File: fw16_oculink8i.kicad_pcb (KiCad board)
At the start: 4 copper layers, 99.3 x 73.9 mm, 78 parts, among them J1 FXBeam, J2 x8 NPIO, J3 USB_A, J4 FAN_CON_L, J5 FAN_CON_R, SW1 SW_DPDT_x2, SW2 SW_DPDT_x2, U1 LM393, U2 BR24G32FVT-3GE2

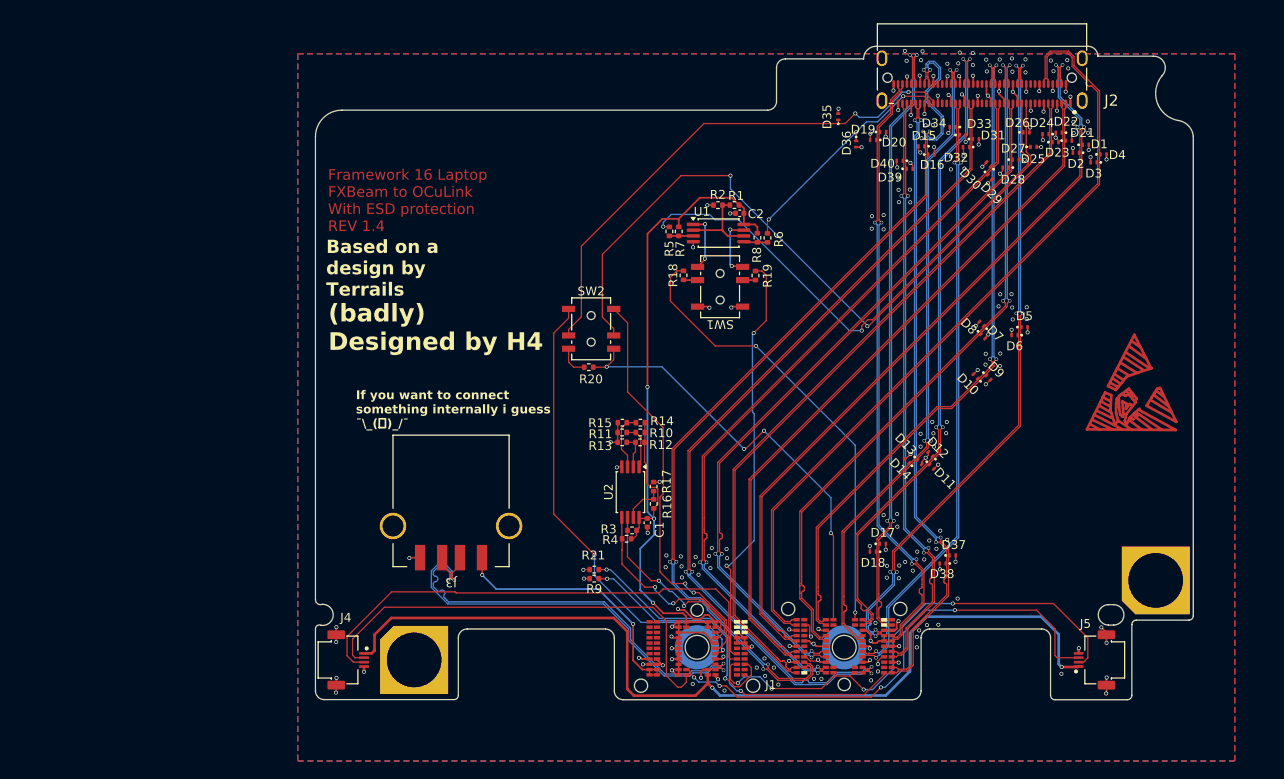
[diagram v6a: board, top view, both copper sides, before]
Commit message: updated routing for JLC04121H-7628 1.2mm PCBs
Because this stackup lets you have cheaper PCBAs.
A bit bigger traces but it should be fine.
Passes ERC, needs a bit more GND vias scattered around.
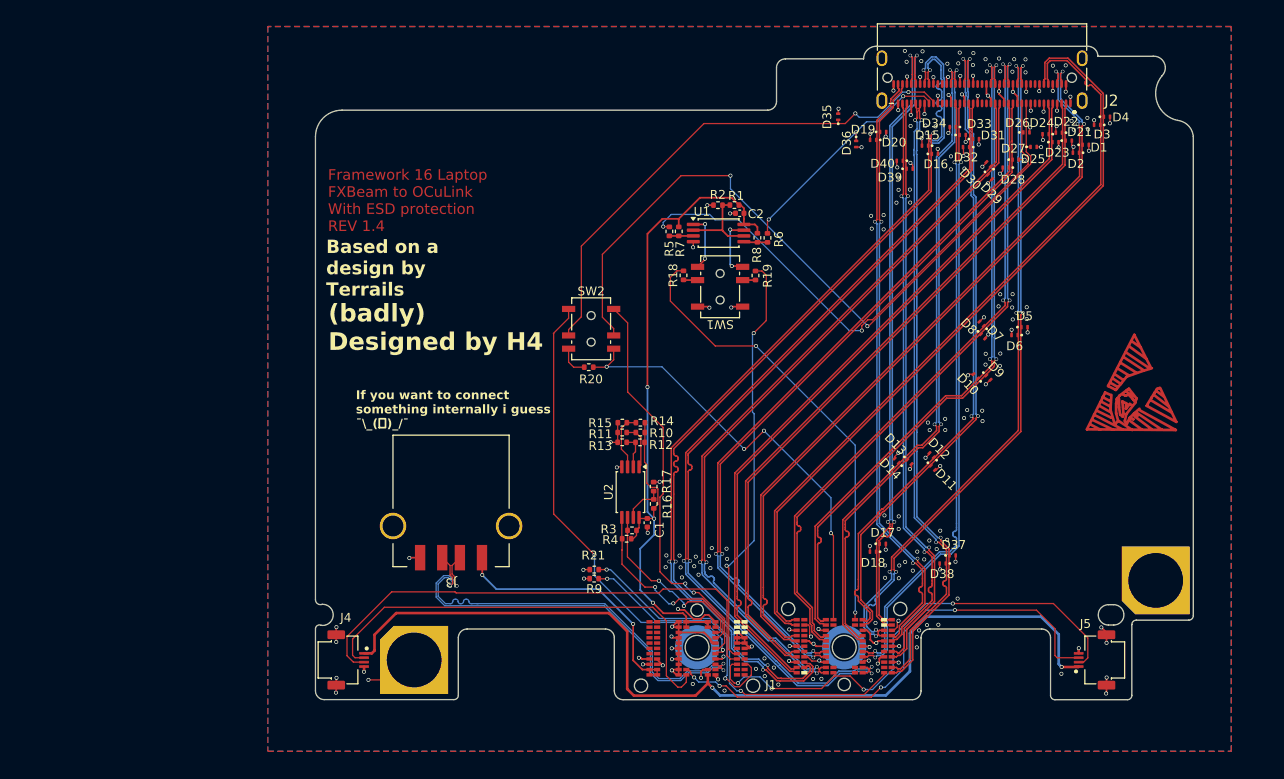
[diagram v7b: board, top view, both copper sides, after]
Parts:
- moved D4 4.28 mm to (145.9, 31.2)
- moved D3 4.26 mm to (144.8, 32.1)
- moved D14 1.16 mm to (122.2, 70.1)
- moved D13 1.16 mm to (123.6, 70.3)
- moved D15 0.41 mm to (125.4, 34.5)
- moved D16 0.41 mm to (126.5, 35.4)
- moved D11 0.18 mm to (126.2, 70.9)
- moved D12 0.18 mm to (126.1, 69.5)
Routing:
- net GND: track 133.0 -> 138.4 mm, vias 218 -> 219
- net /REFCLKB+: track 100.5 -> 103.7 mm
- net /RX1+: track 89.3 -> 87.6 mm
- net /RX1-: track 89.3 -> 87.6 mm
- net /RX0-: track 86.2 -> 84.6 mm
- net /RX0+: track 86.2 -> 84.6 mm
- net /REFCLKB-: track 103.0 -> 103.9 mm
- net /TX5+: track 68.7 -> 69.4 mm
- net /TX5-: track 68.6 -> 69.4 mm
- net /RX2+: track 78.9 -> 79.5 mm
- net /RX2-: track 79.0 -> 79.6 mm

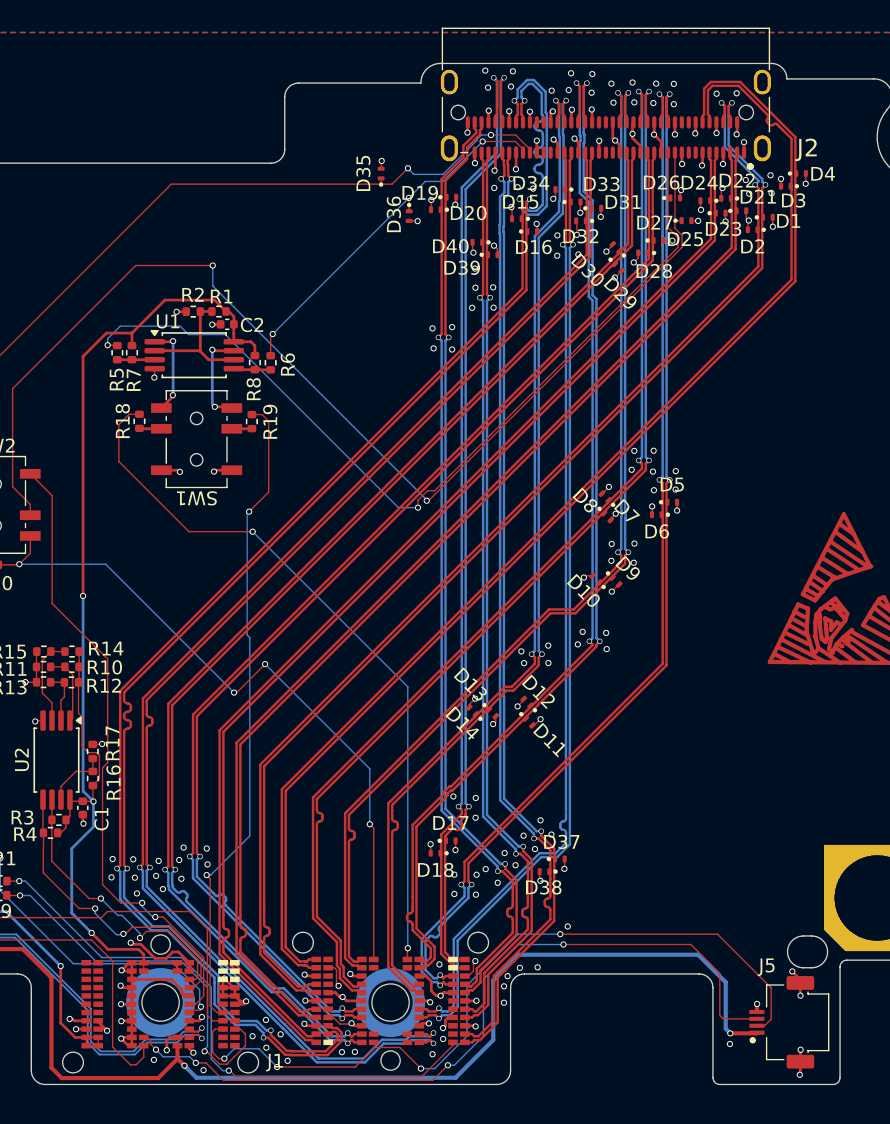
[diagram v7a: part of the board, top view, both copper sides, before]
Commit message: added a whole lot of GND vias
because high frequency so better off playing it safe and annoy JLCPCB production a bit.
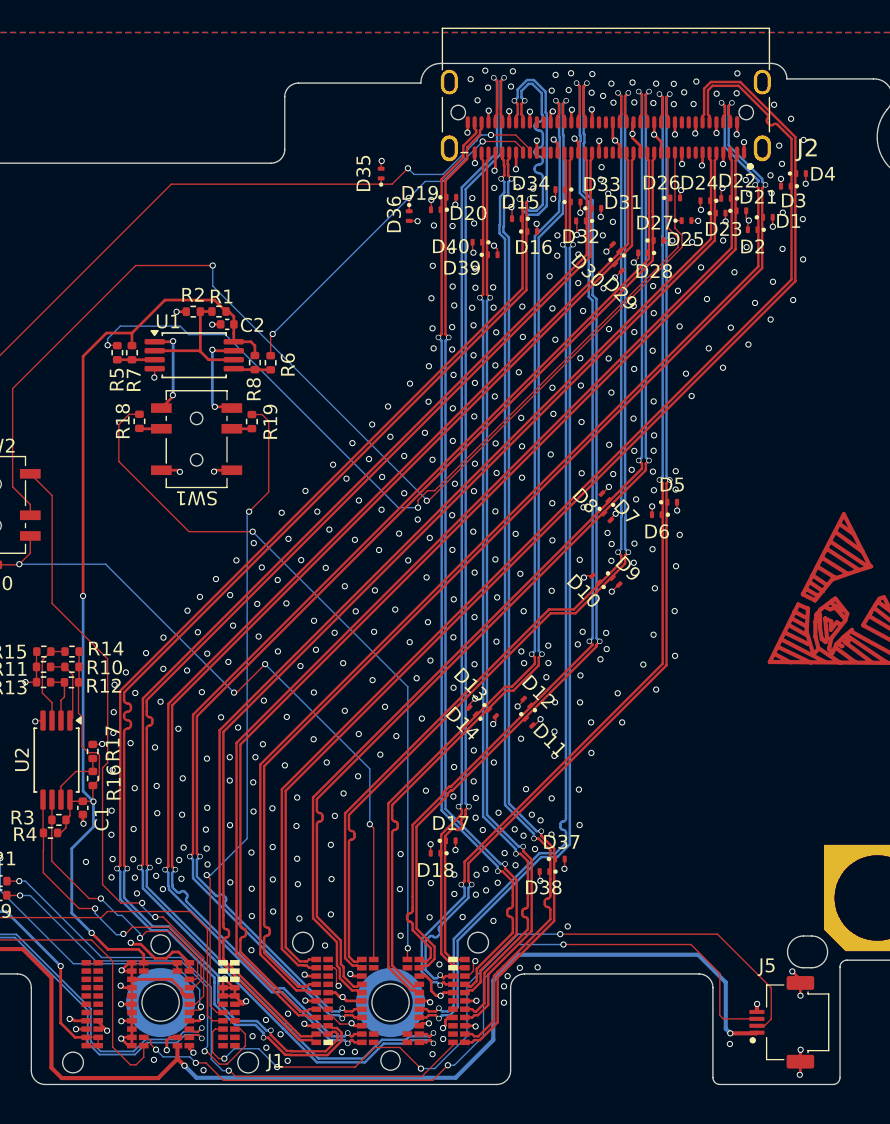
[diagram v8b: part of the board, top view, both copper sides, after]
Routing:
- net GND: vias 219 -> 513
